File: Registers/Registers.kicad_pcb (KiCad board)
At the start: 2 copper layers, 85 x 99.5 mm, 32 parts, among them J1 Output to Display, J2 Reg Specific Connections, J3 LED Wire Bus, J4 LED Wire Bus, U1 74HC173, U2 74HC173, U3 74HC245, U4 ATtiny84-20P

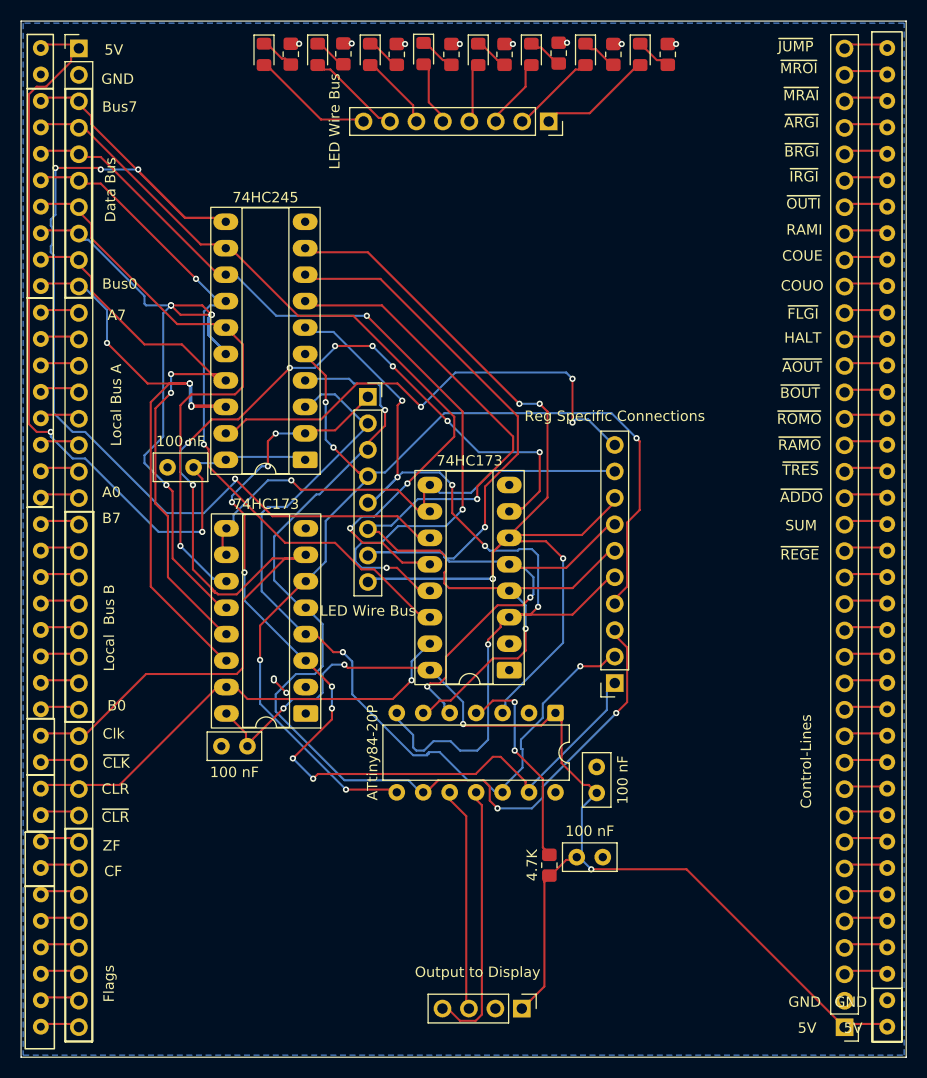
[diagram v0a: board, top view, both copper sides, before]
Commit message: Board version set up without wire jumpers to LEDs
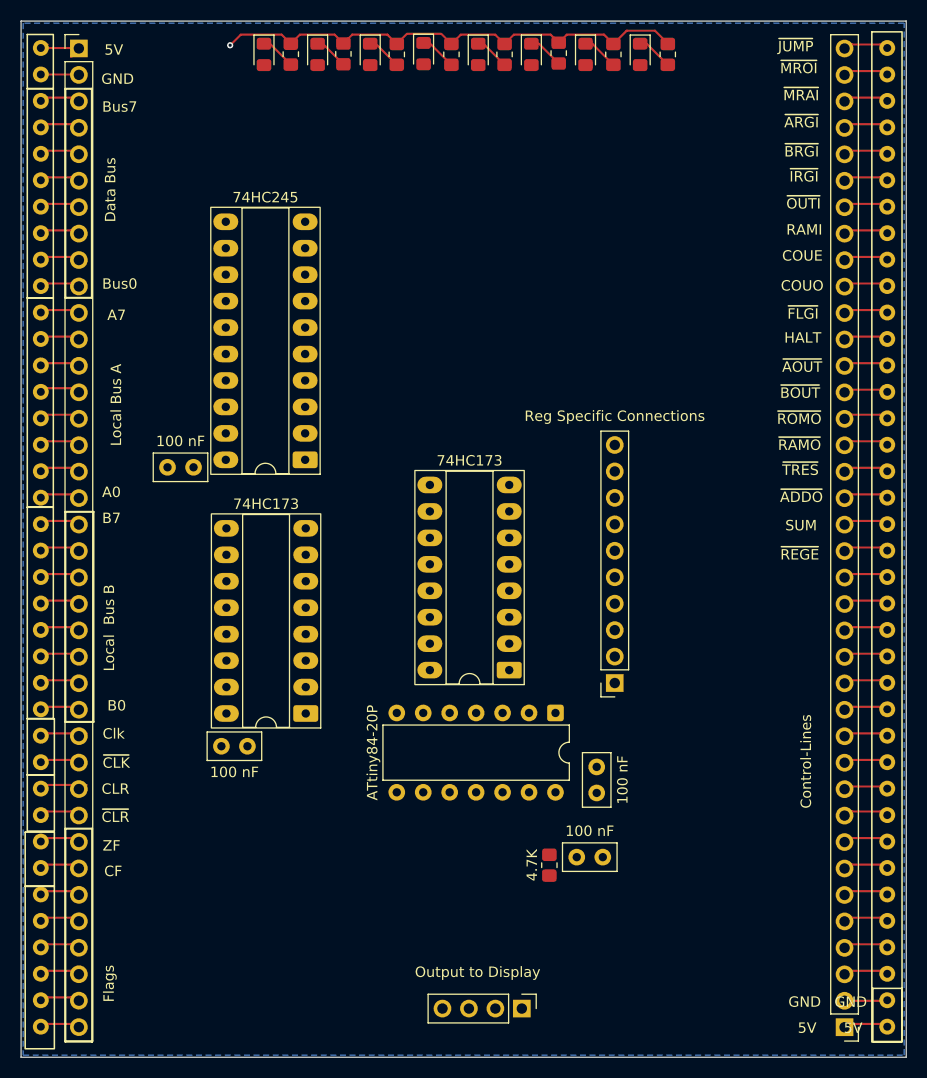
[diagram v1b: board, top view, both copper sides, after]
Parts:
- removed J3, J4: LED Wire Bus, Connector_PinSocket_2.54mm:PinSocket_1x08_P2.54mm_Vertical
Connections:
- D1 pad 2: Net-(D1-A) -> REG7
- D2 pad 2: Net-(D2-A) -> REG6
- D3 pad 2: Net-(D3-A) -> REG5
- D4 pad 2: Net-(D4-A) -> REG4
- D5 pad 2: Net-(D5-A) -> REG3
- D6 pad 2: Net-(D6-A) -> REG2
- D7 pad 2: Net-(D7-A) -> REG1
- D8 pad 2: Net-(D8-A) -> REG0
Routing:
- net REG7: track 111.6 -> 0.00 mm, vias 5 -> 0
- net 5V_2: track 112.2 -> 4.22 mm, vias 4 -> 0
- net CLOCK: track 112.2 -> 4.53 mm, vias 8 -> 0
- net BUS7: track 109.6 -> 3.81 mm, vias 4 -> 0
- net REG3: track 103.4 -> 0.00 mm, vias 5 -> 0
- net REG2: track 100.2 -> 0.00 mm, vias 3 -> 0
- net REG6: track 99.6 -> 0.00 mm, vias 3 -> 0
- net REG5: track 92.2 -> 0.00 mm, vias 2 -> 0
- net REG4: track 90.6 -> 0.00 mm, vias 6 -> 0
- net REG0: track 89.0 -> 0.00 mm, vias 8 -> 0
- net REG1: track 81.1 -> 0.00 mm, vias 2 -> 0
- net BUS5: track 81.4 -> 3.79 mm, vias 3 -> 0
- net 5V: track 81.0 -> 6.36 mm, vias 2 -> 0
- net BUS6: track 75.8 -> 3.80 mm, vias 2 -> 0
- net BUS4: track 67.2 -> 3.78 mm, vias 2 -> 0
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
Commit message: Auto-routed and placed board with some additional text and small manual changes.
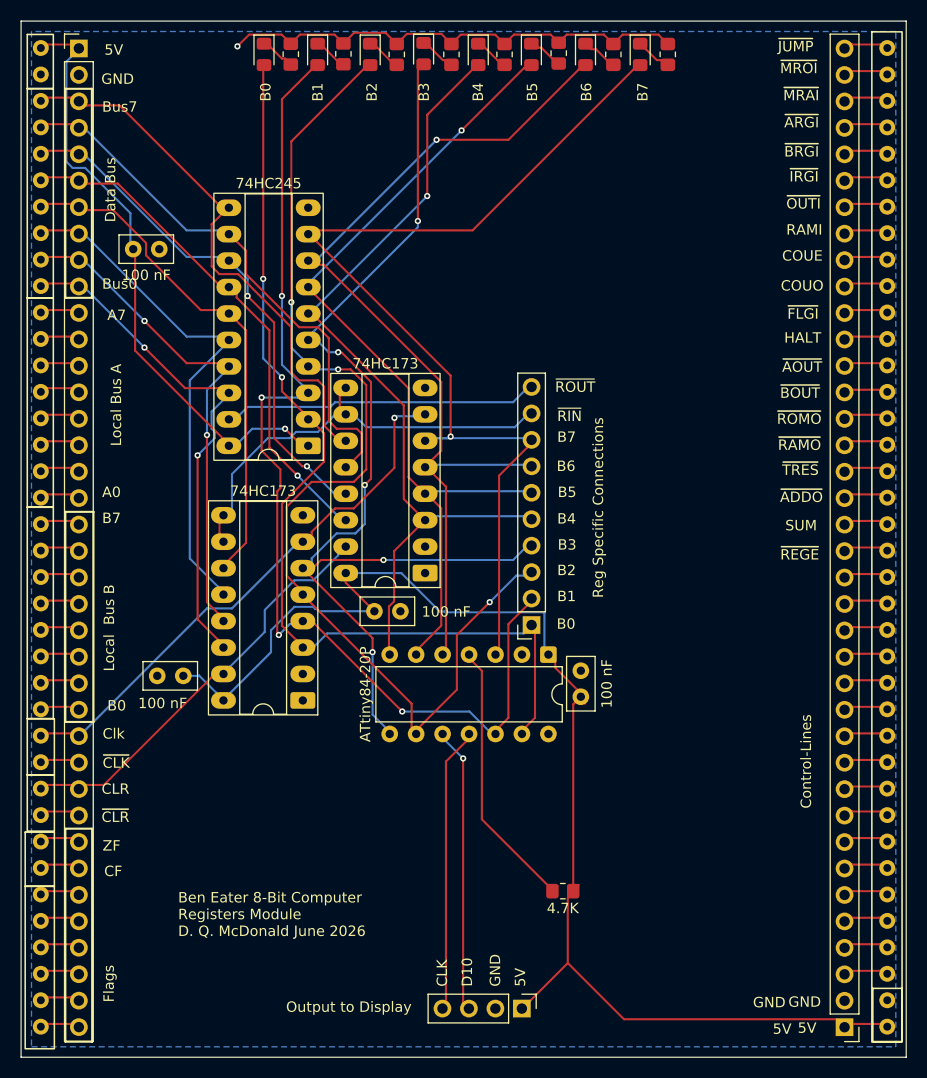
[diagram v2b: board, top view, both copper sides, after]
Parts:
- moved C4 30.6 mm to (60.1, 85.3)
- moved C3 21.7 mm to (34.5, 50.6), turned to 0 degrees
- moved U2 12.3 mm to (62.5, 81.7)
- moved J2 9.74 mm to (72.7, 86.7)
- moved C1 9.36 mm to (77.5, 93.6)
- moved C2 9.15 mm to (36.8, 91.5)
- moved U4 5.64 mm to (74.4, 89.5)
- moved R9 2.81 mm to (75.7, 112.2), turned to 0 degrees
- moved U3 1.38 mm to (51.3, 69.5)
- moved U1 1.29 mm to (50.8, 93.9)
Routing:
- net 5V_2: track 4.22 -> 128.8 mm
- net REG2: track 0.00 -> 103.8 mm, vias 0 -> 3
- net REG3: track 0.00 -> 102.4 mm, vias 0 -> 5
- net REG1: track 0.00 -> 102.2 mm, vias 0 -> 4
- net REG7: track 0.00 -> 98.3 mm, vias 0 -> 1
- net REG0: track 0.00 -> 94.7 mm, vias 0 -> 2
- net REG6: track 0.00 -> 89.8 mm, vias 0 -> 1
- net REG5: track 0.00 -> 82.1 mm, vias 0 -> 1
- net REG4: track 0.00 -> 81.8 mm, vias 0 -> 1
- net 5V: track 6.36 -> 58.2 mm, vias 0 -> 1
- net BUS7: track 3.81 -> 53.1 mm
- net BUS6: track 3.80 -> 52.8 mm
- net CLOCK: track 4.53 -> 52.6 mm, vias 0 -> 1
- net BUS5: track 3.79 -> 50.2 mm, vias 0 -> 2
- net BUS2: track 3.77 -> 49.5 mm
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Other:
- board text added: "B0"
- board text added: "B1"
- board text added: "B2"
- board text added: "B3"
- board text added: "B4"
- board text added: "B5"
- board text added: "B6"
- board text added: "B7"
- board text added: "Ben Eater 8-Bit Computer Registers Module D. Q. McDonald June 2026"
- board text added: "CLK"
- board text added: "D10"
- board text added: "~{RIN}"
- board text added: "~{ROUT}"

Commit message: Reviewed register design - made a few small changes to satisfy the review.
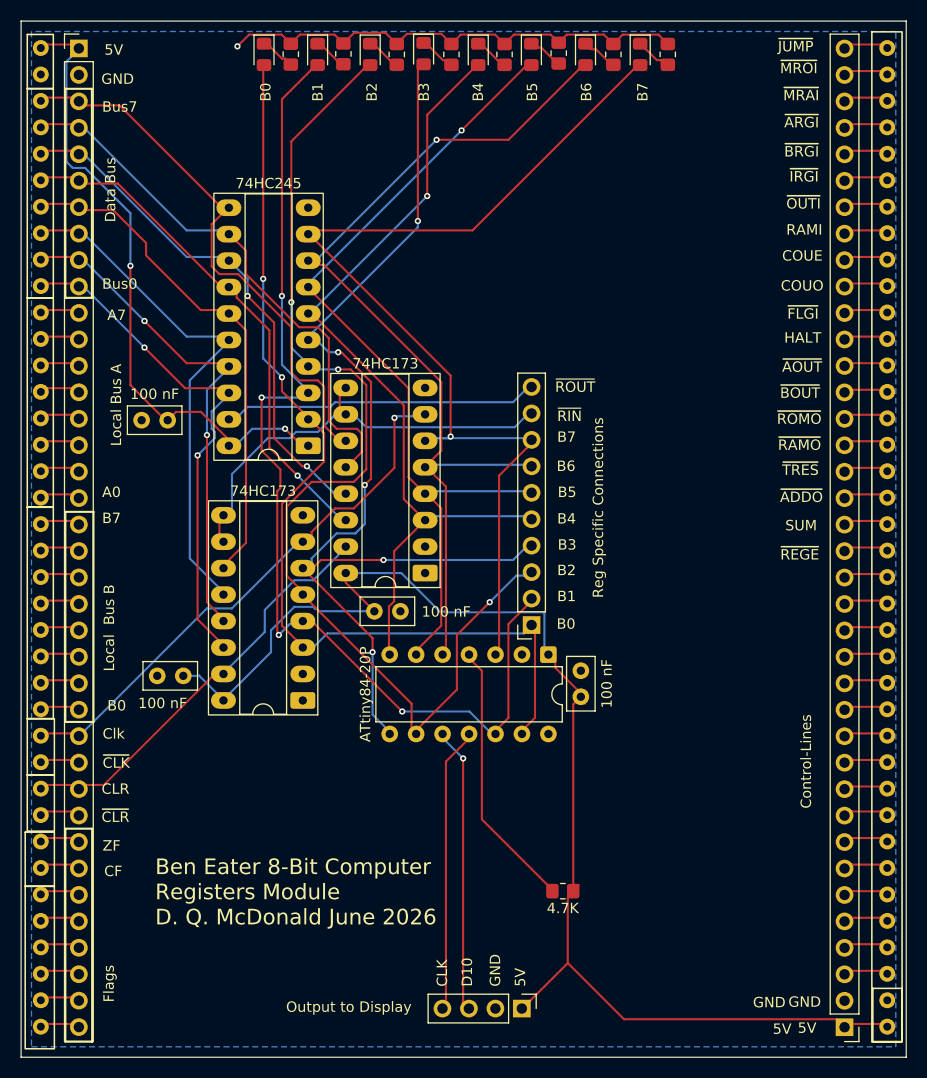
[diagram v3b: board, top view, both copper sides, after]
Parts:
- moved C3 16.8 mm to (37.8, 67.0), turned to 180 degrees
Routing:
- net 5V: track 58.2 -> 62.5 mm, vias 1 -> 2
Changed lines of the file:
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@@
 	(footprint "Capacitor_THT:C_Disc_D5.0mm_W2.5mm_P2.50mm"
 		(layer "F.Cu")
-		(at 34.495267 50.573553)
+		(at 37.8 67 180)
 		(descr "C, Disc series, Radial, pin pitch=2.50mm, diameter*width=5*2.5mm^2, Capacitor, http://cdn-reichelt.de/documents/datenblatt/B300/DS_KERKO_TC.pdf")
 		(tags "C Disc series Radial pin pitch 2.50mm diameter 5mm width 2.5mm Capacitor")
 		(property "Reference" "C3"
-			(at 0.59 -7 180)
+			(at 0.59 -7 0)
 			(layer "F.Fab")
 			(effects
@@
 		)
 		(property "Value" "100 nF"
-			(at 1.25 2.5 180)
+			(at 1.25 2.5 0)
 			(layer "F.SilkS")
 			(effects
@@
 		)
 		(property "Datasheet" ""
-			(at 0 0 180)
+			(at 0 0 0)
 			(layer "F.Fab")
 			(hide yes)
@@
 		)
 		(property "Description" "Unpolarized capacitor, small symbol"
-			(at 0 0 180)
+			(at 0 0 0)
 			(layer "F.Fab")
 			(hide yes)
@@
 		)
 		(property "MPN" "C315C104M5U5TA"
-			(at 0 0 0)
+			(at 0 0 180)
 			(unlocked yes)
 			(layer "F.Fab")
@@
 		(duplicate_pad_numbers_are_jumpers no)
 		(fp_line
-			(start -1.37 -1.37)
-			(end 3.87 -1.37)
+			(start 3.87 1.37)
+			(end -1.37 1.37)
 			(stroke
 				(width 0.12)
@@
 		)
 		(fp_line
-			(start -1.37 1.37)
-			(end -1.37 -1.37)
+			(start 3.87 -1.37)
+			(end 3.87 1.37)
 			(stroke
 				(width 0.12)
@@
 		)
 		(fp_line
-			(start 3.87 -1.37)
-			(end 3.87 1.37)
+			(start -1.37 1.37)
+			(end -1.37 -1.37)
 			(stroke
 				(width 0.12)
@@
 		)
 		(fp_line
-			(start 3.87 1.37)
-			(end -1.37 1.37)
+			(start -1.37 -1.37)
+			(end 3.87 -1.37)
 			(stroke
 				(width 0.12)
@@
 		)
 		(fp_text user "${REFERENCE}"
-			(at 1.25 0 180)
+			(at 1.25 0 0)
 			(layer "F.Fab")
 			(effects
@@
 		)
 		(pad "1" thru_hole circle
-			(at 0 0)
+			(at 0 0 180)
 			(size 1.6 1.6)
 			(drill 0.8)
@@
 		)
 		(pad "2" thru_hole circle
-			(at 2.5 0)
+			(at 2.5 0 180)
 			(size 1.6 1.6)
 			(drill 0.8)
@@
 		(layer "Edge.Cuts")
 	)
-	(gr_text "Ben Eater 8-Bit Computer\nRegisters Module\nD. Q. McDonald June 2026"
-		(at 38.8 116.65 0)
-		(layer "F.SilkS")
-		(effects
-			(font
-				(size 1 1)
-				(thickness 0.1)
-			)
-			(justify left bottom)
-		)
-	)
 	(gr_text "~{ROUT}"
 		(at 75 64.4 0)
@@
 		)
 	)
+	(gr_text "Ben Eater 8-Bit Computer\nRegisters Module\nD. Q. McDonald June 2026"
+		(at 36.6 115.6 0)
+		(layer "F.SilkS")
+		(effects
+			(font
+				(size 1.5 1.5)
+				(thickness 0.1)
+			)
+			(justify left bottom)
+		)
+	)
 	(segment
 		(start 65.050104 32.875)
@@
 	)
 	(segment
-		(start 34.495267 50.573553)
-		(end 34.675 51.325)
+		(start 37.6 67)
+		(end 37.8 67)
 		(width 0.2)
 		(layer "F.Cu")
@@
 	)
 	(segment
-		(start 43.075 68.725)
-		(end 34.675 60.325)
+		(start 34.225 52.175)
+		(end 34.225 63.625)
 		(width 0.2)
 		(layer "F.Cu")
@@
 	)
 	(segment
-		(start 43.67814 69.45802)
-		(end 43.075 68.725)
+		(start 41.004485 66.2)
+		(end 43.67814 68.873655)
+		(width 0.2)
+		(layer "F.Cu")
+		(net "5V")
+	)
+	(segment
+		(start 37.8 67)
+		(end 38.6 66.2)
+		(width 0.2)
+		(layer "F.Cu")
+		(net "5V")
+	)
+	(segment
+		(start 43.67814 68.873655)
+		(end 43.67814 69.45802)
 		(width 0.2)
 		(layer "F.Cu")
@@
 	)
 	(segment
+		(start 34.225 63.625)
+		(end 37.6 67)
+		(width 0.2)
+		(layer "F.Cu")
+		(net "5V")
+	)
+	(segment
 		(start 51.29814 69.45802)
 		(end 50.125 68.875)
@@
 	)
 	(segment
-		(start 34.675 60.325)
-		(end 34.675 51.325)
+		(start 38.6 66.2)
+		(end 41.004485 66.2)
+		(width 0.2)
+		(layer "F.Cu")
+		(net "5V")
+	)
+	(segment
+		(start 43.075 68.725)
+		(end 43.67814 69.45802)
 		(width 0.2)
 		(layer "F.Cu")
@@
 	)
 	(via
+		(at 34.225 52.175)
+		(size 0.6)
+		(drill 0.3)
+		(layers "F.Cu" "B.Cu")
+		(net "5V")
+	)
+	(via
 		(at 49.075 67.825)
 		(size 0.6)
@@
 	)
 	(segment
-		(start 29.275 31.3)
-		(end 28.525 32.125)
+		(start 34.2 52.2)
+		(end 34.225 52.175)
 		(width 0.2)
 		(layer "B.Cu")
@@
 	)
 	(segment
-		(start 34.495267 50.573553)
-		(end 34.225 49.825)
+		(start 29.275 31.3)
+		(end 28.525 32.125)
 		(width 0.2)
 		(layer "B.Cu")
@@
 	)
 	(segment
-		(start 34.225 49.825)
-		(end 34.225 47.125)
+		(start 34.225 47.125)
+		(end 34.225 52.175)
 		(width 0.2)
 		(layer "B.Cu")

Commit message: [Registers]  - Version ready for manufacture.
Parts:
- added R10: 10K, Resistor_SMD:R_0805_2012Metric_Pad1.20x1.40mm_HandSolder, F.Cu at (83.1, 89.0)
- added R11: 10K, Resistor_SMD:R_0805_2012Metric_Pad1.20x1.40mm_HandSolder, F.Cu at (83.1, 86.1)
- added R12: 10K, Resistor_SMD:R_0805_2012Metric_Pad1.20x1.40mm_HandSolder, F.Cu at (83.1, 83.2)
- added R13: 10K, Resistor_SMD:R_0805_2012Metric_Pad1.20x1.40mm_HandSolder, F.Cu at (83.1, 80.2)
- added R14: 10K, Resistor_SMD:R_0805_2012Metric_Pad1.20x1.40mm_HandSolder, F.Cu at (83.1, 77.2)
- added R15: 10K, Resistor_SMD:R_0805_2012Metric_Pad1.20x1.40mm_HandSolder, F.Cu at (83.1, 74.3)
- added R16: 10K, Resistor_SMD:R_0805_2012Metric_Pad1.20x1.40mm_HandSolder, F.Cu at (83.1, 71.0)
- added R17: 10K, Resistor_SMD:R_0805_2012Metric_Pad1.20x1.40mm_HandSolder, F.Cu at (83.1, 68.0)
- added R18: 10K, Resistor_SMD:R_0805_2012Metric_Pad1.20x1.40mm_HandSolder, F.Cu at (83.1, 65.1)
- added R19: 10K, Resistor_SMD:R_0805_2012Metric_Pad1.20x1.40mm_HandSolder, F.Cu at (83.1, 62.1)
- R1, R2, R3, R4, R5, R6, R7, R8: value 220 Ohm -> 330R
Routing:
- net 5V_2: track 128.8 -> 203.6 mm
- net GND: track 47.7 -> 72.9 mm, vias 1 -> 2
- net REG0: track 94.7 -> 105.0 mm
- net REG1: track 102.2 -> 112.4 mm
- net ~{ROUT}: track 30.2 -> 40.2 mm
- net REG2: track 103.8 -> 113.8 mm
- net ~{RIN}: track 42.0 -> 51.9 mm
- net REG3: track 102.4 -> 112.2 mm
- net REG7: track 98.3 -> 108.0 mm
- net REG4: track 81.8 -> 91.4 mm
- net REG6: track 89.8 -> 99.3 mm
- net REG5: track 82.1 -> 91.6 mm
